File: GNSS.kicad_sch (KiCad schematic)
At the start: 0 parts

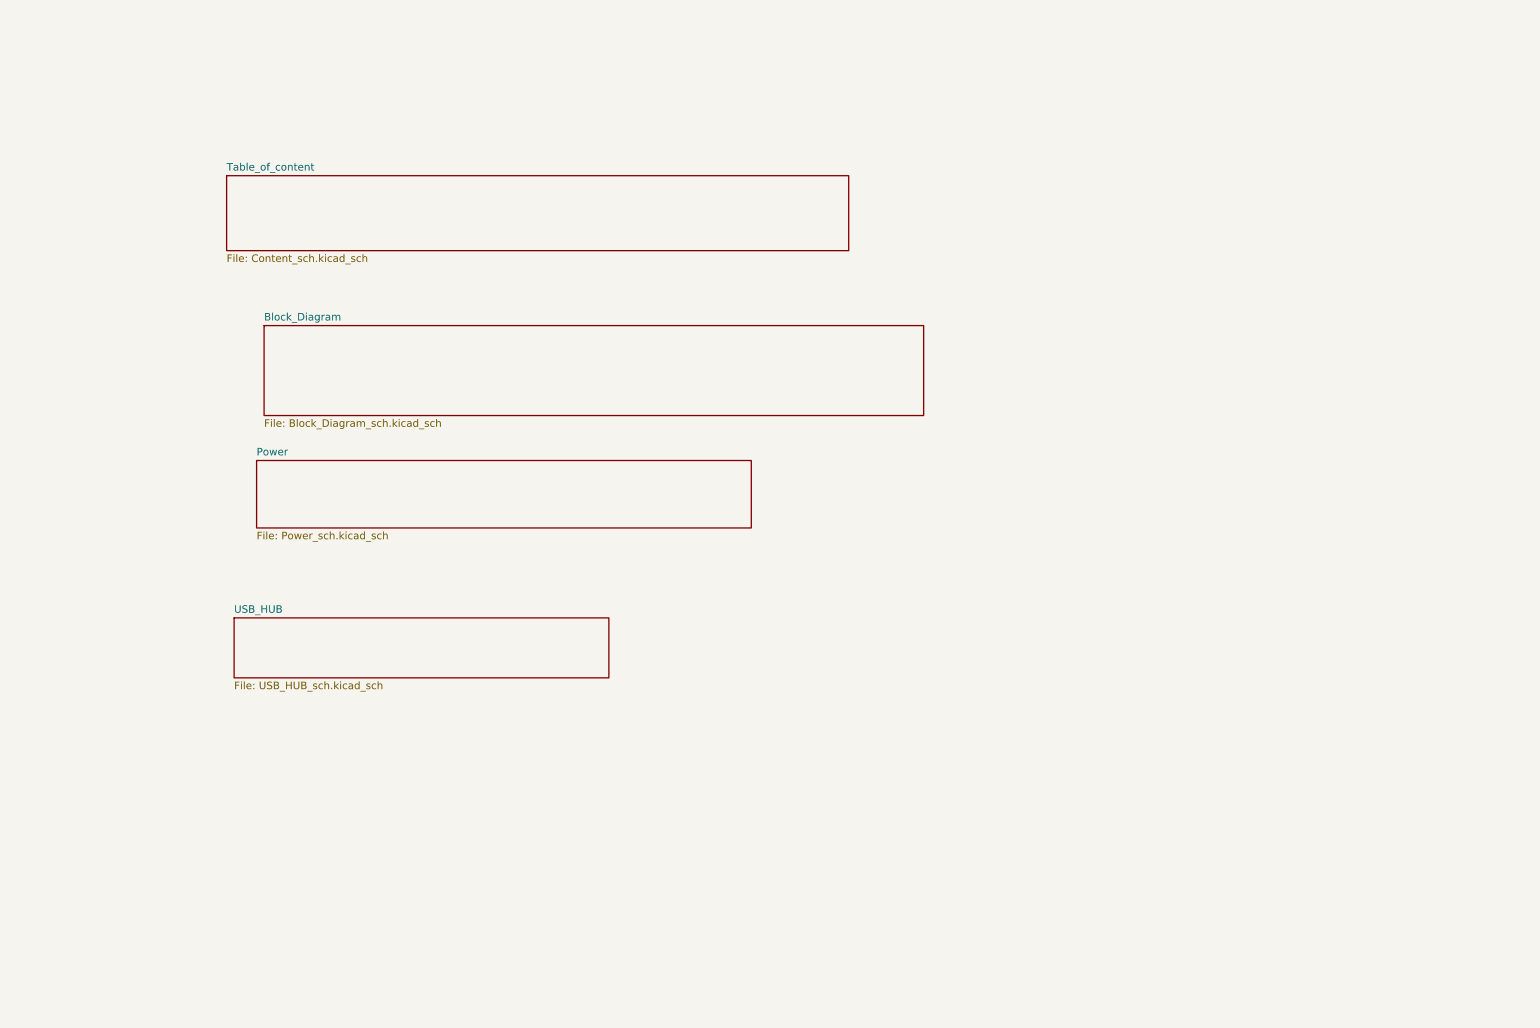
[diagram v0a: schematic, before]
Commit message: update the power sheet
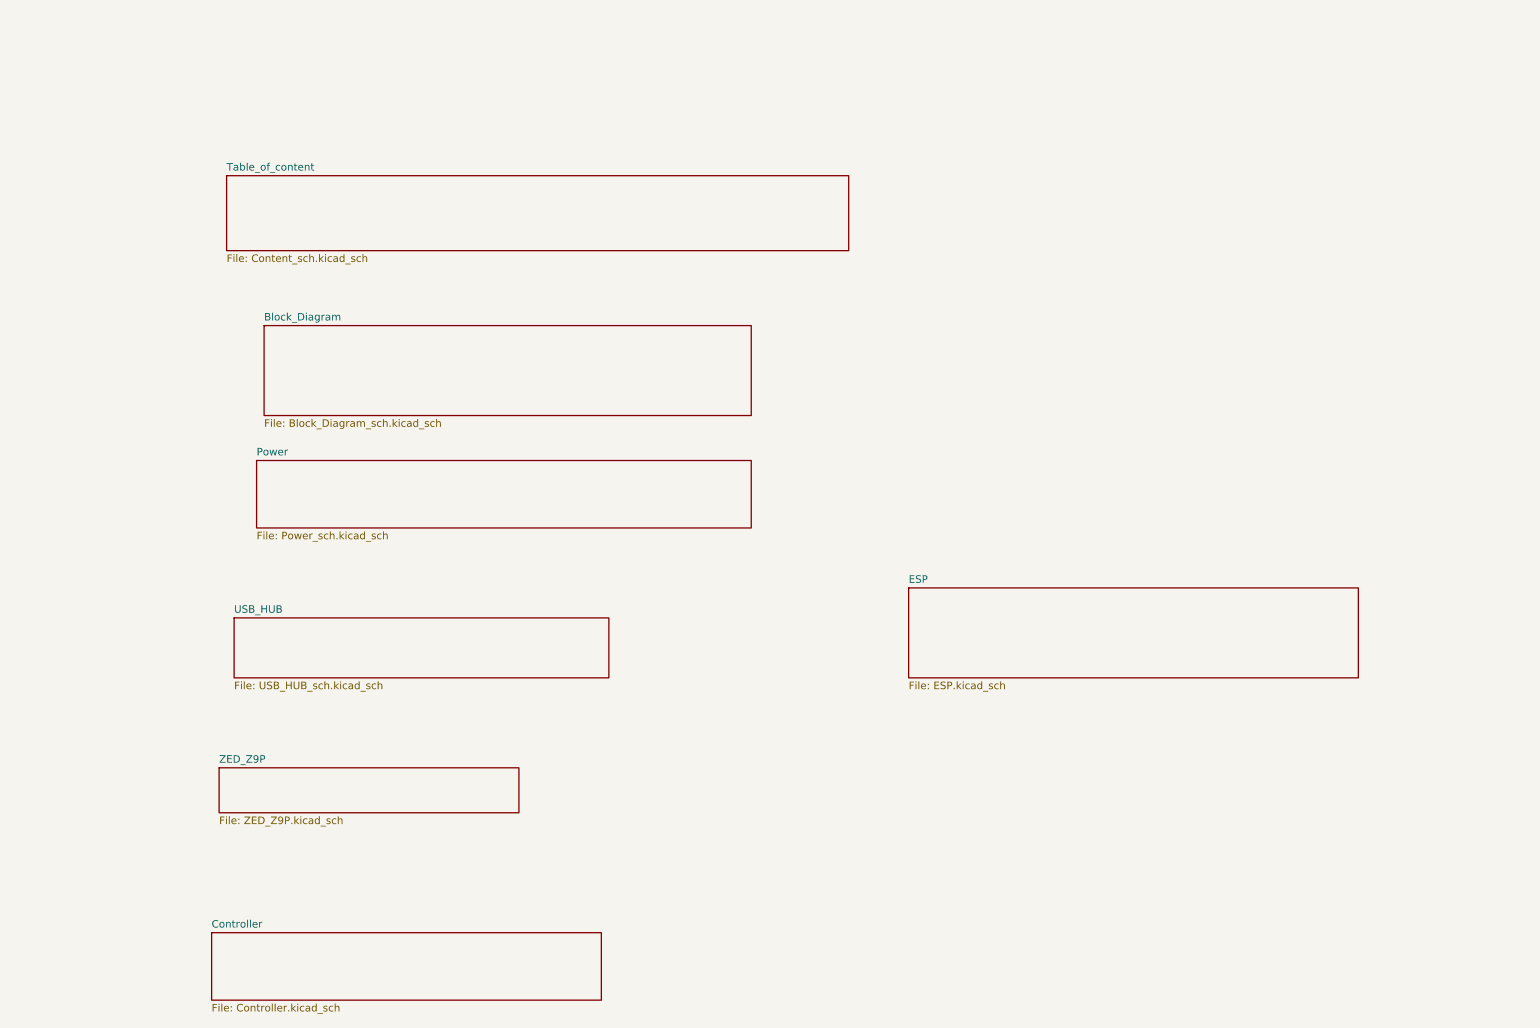
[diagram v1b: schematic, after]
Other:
- added sheet Controller (Controller.kicad_sch)
- added sheet ESP (ESP.kicad_sch)
- added sheet ZED_Z9P (ZED_Z9P.kicad_sch)
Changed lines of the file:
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@@
+	)
+	(sheet
+		(at 55.88 143.51)
+		(size 50.8 7.62)
+		(fields_autoplaced yes)
+		(stroke
+			(width 0.1524)
+			(type solid)
+		)
+		(fill
+			(color 0 0 0 0.0000)
+		)
+		(property "Sheetname" "ZED_Z9P"
+			(at 55.88 142.7984 0)
+			(effects
+				(font
+					(size 1.27 1.27)
+				)
+				(justify left bottom)
+			)
+		)
+		(property "Sheetfile" "ZED_Z9P.kicad_sch"
+			(at 55.88 151.7146 0)
+			(effects
+				(font
+					(size 1.27 1.27)
+				)
+				(justify left top)
+			)
+		)
+		(instances
+			(project "GNSS"
+				(path "/a70dad34-b24c-4b58-b91c-f14576b5da7d"
+					(page "6")
+				)
+			)
+		)
 	)
 	(sheet
@@
 	)
 	(sheet
+		(at 54.61 171.45)
+		(size 66.04 11.43)
+		(fields_autoplaced yes)
+		(stroke
+			(width 0.1524)
+			(type solid)
+		)
+		(fill
+			(color 0 0 0 0.0000)
+		)
+		(property "Sheetname" "Controller"
+			(at 54.61 170.7384 0)
+			(effects
+				(font
+					(size 1.27 1.27)
+				)
+				(justify left bottom)
+			)
+		)
+		(property "Sheetfile" "Controller.kicad_sch"
+			(at 54.61 183.4646 0)
+			(effects
+				(font
+					(size 1.27 1.27)
+				)
+				(justify left top)
+			)
+		)
+		(instances
+			(project "GNSS"
+				(path "/a70dad34-b24c-4b58-b91c-f14576b5da7d"
+					(page "7")
+				)
+			)
+		)
+	)
+	(sheet
 		(at 63.5 68.58)
-		(size 111.76 15.24)
+		(size 82.55 15.24)
 		(fields_autoplaced yes)
 		(stroke
@@
 				)
 			)
+		)
+	)
+	(sheet
+		(at 172.72 113.03)
+		(size 76.2 15.24)
+		(fields_autoplaced yes)
+		(stroke
+			(width 0.1524)
+			(type solid)
+		)
+		(fill
+			(color 0 0 0 0.0000)
+		)
+		(property "Sheetname" "ESP"
+			(at 172.72 112.3184 0)
+			(effects
+				(font
+					(size 1.27 1.27)
+				)
+				(justify left bottom)
+			)
+		)
+		(property "Sheetfile" "ESP.kicad_sch"
+			(at 172.72 128.8546 0)
+			(effects
+				(font
+					(size 1.27 1.27)
+				)
+				(justify left top)
+			)
+		)
+		(instances
+			(project "GNSS"
+				(path "/a70dad34-b24c-4b58-b91c-f14576b5da7d"
+					(page "8")
+				)
+			)

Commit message: arrange the Sheets
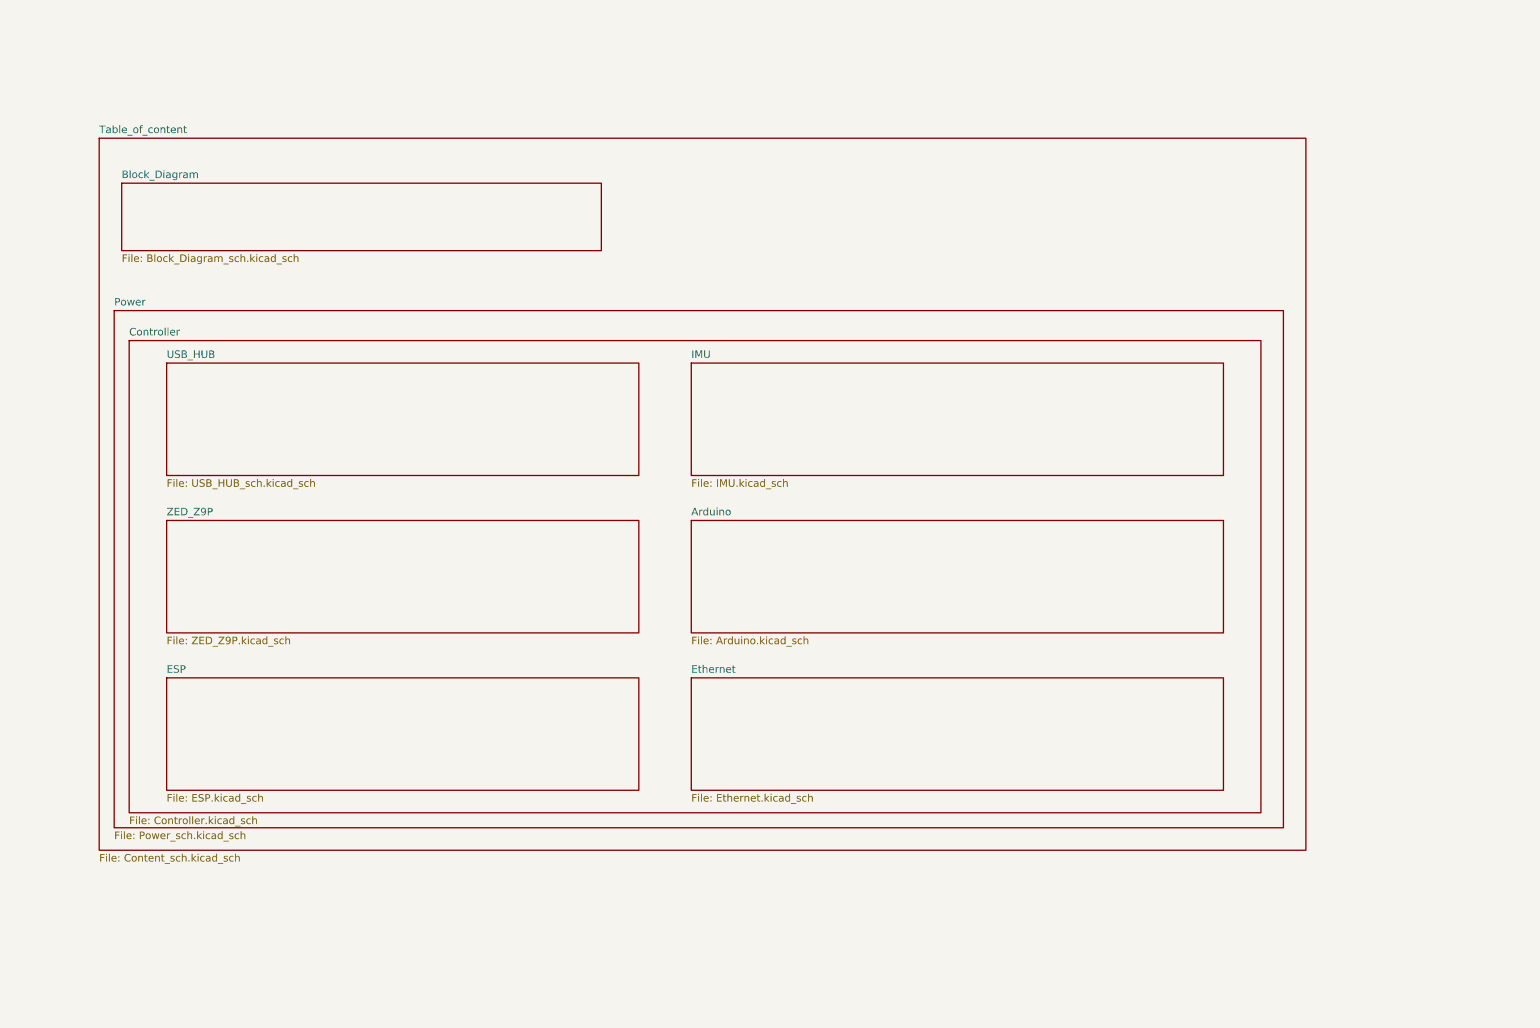
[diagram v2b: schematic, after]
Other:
- added sheet Arduino (Arduino.kicad_sch)
- added sheet Ethernet (Ethernet.kicad_sch)
- added sheet IMU (IMU.kicad_sch)
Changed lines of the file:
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@@
 	(paper "A4")
 	(sheet
-		(at 57.15 43.18)
-		(size 105.41 12.7)
+		(at 35.56 36.83)
+		(size 204.47 120.65)
 		(fields_autoplaced yes)
 		(stroke
@@
 		)
 		(property "Sheetname" "Table_of_content"
-			(at 57.15 42.4684 0)
+			(at 35.56 36.1184 0)
 			(effects
 				(font
@@
 		)
 		(property "Sheetfile" "Content_sch.kicad_sch"
-			(at 57.15 56.4646 0)
+			(at 35.56 158.0646 0)
 			(effects
 				(font
@@
 	)
 	(sheet
-		(at 55.88 143.51)
-		(size 50.8 7.62)
+		(at 135.89 74.93)
+		(size 90.17 19.05)
+		(fields_autoplaced yes)
+		(stroke
+			(width 0.1524)
+			(type solid)
+		)
+		(fill
+			(color 0 0 0 0.0000)
+		)
+		(property "Sheetname" "IMU"
+			(at 135.89 74.2184 0)
+			(effects
+				(font
+					(size 1.27 1.27)
+				)
+				(justify left bottom)
+			)
+		)
+		(property "Sheetfile" "IMU.kicad_sch"
+			(at 135.89 94.5646 0)
+			(effects
+				(font
+					(size 1.27 1.27)
+				)
+				(justify left top)
+			)
+		)
+		(instances
+			(project "GNSS"
+				(path "/a70dad34-b24c-4b58-b91c-f14576b5da7d"
+					(page "11")
+				)
+			)
+		)
+	)
+	(sheet
+		(at 46.99 101.6)
+		(size 80.01 19.05)
 		(fields_autoplaced yes)
 		(stroke
@@
 		)
 		(property "Sheetname" "ZED_Z9P"
-			(at 55.88 142.7984 0)
+			(at 46.99 100.8884 0)
 			(effects
 				(font
@@
 		)
 		(property "Sheetfile" "ZED_Z9P.kicad_sch"
-			(at 55.88 151.7146 0)
+			(at 46.99 121.2346 0)
 			(effects
 				(font
@@
 	)
 	(sheet
-		(at 58.42 118.11)
-		(size 63.5 10.16)
+		(at 46.99 74.93)
+		(size 80.01 19.05)
 		(fields_autoplaced yes)
 		(stroke
@@
 		)
 		(property "Sheetname" "USB_HUB"
-			(at 58.42 117.3984 0)
+			(at 46.99 74.2184 0)
 			(effects
 				(font
@@
 		)
 		(property "Sheetfile" "USB_HUB_sch.kicad_sch"
-			(at 58.42 128.8546 0)
+			(at 46.99 94.5646 0)
 			(effects
 				(font
@@
 	)
 	(sheet
-		(at 54.61 171.45)
-		(size 66.04 11.43)
+		(at 40.64 71.12)
+		(size 191.77 80.01)
 		(fields_autoplaced yes)
 		(stroke
@@
 		)
 		(property "Sheetname" "Controller"
-			(at 54.61 170.7384 0)
+			(at 40.64 70.4084 0)
 			(effects
 				(font
@@
 		)
 		(property "Sheetfile" "Controller.kicad_sch"
-			(at 54.61 183.4646 0)
+			(at 40.64 151.7146 0)
 			(effects
 				(font
@@
 	)
 	(sheet
-		(at 63.5 68.58)
-		(size 82.55 15.24)
+		(at 39.37 44.45)
+		(size 81.28 11.43)
 		(fields_autoplaced yes)
 		(stroke
@@
 		)
 		(property "Sheetname" "Block_Diagram"
-			(at 63.5 67.8684 0)
+			(at 39.37 43.7384 0)
 			(effects
 				(font
@@
 		)
 		(property "Sheetfile" "Block_Diagram_sch.kicad_sch"
-			(at 63.5 84.4046 0)
+			(at 39.37 56.4646 0)
 			(effects
 				(font
@@
 	)
 	(sheet
-		(at 62.23 91.44)
-		(size 83.82 11.43)
+		(at 38.1 66.04)
+		(size 198.12 87.63)
 		(fields_autoplaced yes)
 		(stroke
@@
 		)
 		(property "Sheetname" "Power"
-			(at 62.23 90.7284 0)
+			(at 38.1 65.3284 0)
 			(effects
 				(font
@@
 		)
 		(property "Sheetfile" "Power_sch.kicad_sch"
-			(at 62.23 103.4546 0)
+			(at 38.1 154.2546 0)
 			(effects
 				(font
@@
 	)
 	(sheet
-		(at 172.72 113.03)
-		(size 76.2 15.24)
+		(at 135.89 128.27)
+		(size 90.17 19.05)
+		(fields_autoplaced yes)
+		(stroke
+			(width 0.1524)
+			(type solid)
+		)
+		(fill
+			(color 0 0 0 0.0000)
+		)
+		(property "Sheetname" "Ethernet"
+			(at 135.89 127.5584 0)
+			(effects
+				(font
+					(size 1.27 1.27)
+				)
+				(justify left bottom)
+			)
+		)
+		(property "Sheetfile" "Ethernet.kicad_sch"
+			(at 135.89 147.9046 0)
+			(effects
+				(font
+					(size 1.27 1.27)
+				)
+				(justify left top)
+			)
+		)
+		(instances
+			(project "GNSS"
+				(path "/a70dad34-b24c-4b58-b91c-f14576b5da7d"
+					(page "10")
+				)
+			)
+		)
+	)
+	(sheet
+		(at 135.89 101.6)
+		(size 90.17 19.05)
+		(fields_autoplaced yes)
+		(stroke
+			(width 0.1524)
+			(type solid)
+		)
+		(fill
+			(color 0 0 0 0.0000)
+		)
+		(property "Sheetname" "Arduino"
+			(at 135.89 100.8884 0)
+			(effects
+				(font
+					(size 1.27 1.27)
+				)
+				(justify left bottom)
+			)
+		)
+		(property "Sheetfile" "Arduino.kicad_sch"
+			(at 135.89 121.2346 0)
+			(effects
+				(font
+					(size 1.27 1.27)
+				)
+				(justify left top)
+			)
+		)
+		(instances
+			(project "GNSS"
+				(path "/a70dad34-b24c-4b58-b91c-f14576b5da7d"
+					(page "9")
+				)
+			)
+		)
+	)
+	(sheet
+		(at 46.99 128.27)
+		(size 80.01 19.05)
 		(fields_autoplaced yes)
 		(stroke
@@
 		)
 		(property "Sheetname" "ESP"
-			(at 172.72 112.3184 0)
+			(at 46.99 127.5584 0)
 			(effects
 				(font
@@
 		)
 		(property "Sheetfile" "ESP.kicad_sch"
-			(at 172.72 128.8546 0)
-			(effects
-				(font
+			(at 46.99 147.9046 0)
+			(effects
+				(font

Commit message: new
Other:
- added sheet Power_Architecture (Power_Architecture.kicad_sch)
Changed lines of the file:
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@@
 	(paper "A4")
 	(sheet
-		(at 35.56 36.83)
-		(size 204.47 120.65)
+		(at 36.83 21.59)
+		(size 204.47 137.16)
 		(fields_autoplaced yes)
 		(stroke
@@
 		)
 		(property "Sheetname" "Table_of_content"
-			(at 35.56 36.1184 0)
+			(at 36.83 20.8784 0)
 			(effects
 				(font
@@
 		)
 		(property "Sheetfile" "Content_sch.kicad_sch"
-			(at 35.56 158.0646 0)
+			(at 36.83 159.3346 0)
 			(effects
 				(font
@@
 	)
 	(sheet
-		(at 135.89 74.93)
+		(at 137.16 74.93)
 		(size 90.17 19.05)
 		(fields_autoplaced yes)
@@
 		)
 		(property "Sheetname" "IMU"
-			(at 135.89 74.2184 0)
+			(at 137.16 74.2184 0)
 			(effects
 				(font
@@
 		)
 		(property "Sheetfile" "IMU.kicad_sch"
-			(at 135.89 94.5646 0)
+			(at 137.16 94.5646 0)
 			(effects
 				(font
@@
 	)
 	(sheet
-		(at 46.99 101.6)
+		(at 48.26 101.6)
 		(size 80.01 19.05)
 		(fields_autoplaced yes)
@@
 		)
 		(property "Sheetname" "ZED_Z9P"
-			(at 46.99 100.8884 0)
+			(at 48.26 100.8884 0)
 			(effects
 				(font
@@
 		)
 		(property "Sheetfile" "ZED_Z9P.kicad_sch"
-			(at 46.99 121.2346 0)
+			(at 48.26 121.2346 0)
 			(effects
 				(font
@@
 	)
 	(sheet
-		(at 46.99 74.93)
+		(at 48.26 74.93)
 		(size 80.01 19.05)
 		(fields_autoplaced yes)
@@
 		)
 		(property "Sheetname" "USB_HUB"
-			(at 46.99 74.2184 0)
+			(at 48.26 74.2184 0)
 			(effects
 				(font
@@
 		)
 		(property "Sheetfile" "USB_HUB_sch.kicad_sch"
-			(at 46.99 94.5646 0)
+			(at 48.26 94.5646 0)
 			(effects
 				(font
@@
 	)
 	(sheet
-		(at 40.64 71.12)
+		(at 43.18 53.34)
+		(size 71.12 11.43)
+		(fields_autoplaced yes)
+		(stroke
+			(width 0.1524)
+			(type solid)
+		)
+		(fill
+			(color 0 0 0 0.0000)
+		)
+		(property "Sheetname" "Power_Architecture"
+			(at 43.18 52.6284 0)
+			(effects
+				(font
+					(size 1.27 1.27)
+				)
+				(justify left bottom)
+			)
+		)
+		(property "Sheetfile" "Power_Architecture.kicad_sch"
+			(at 43.18 65.3546 0)
+			(effects
+				(font
+					(size 1.27 1.27)
+				)
+				(justify left top)
+			)
+		)
+		(instances
+			(project "GNSS"
+				(path "/a70dad34-b24c-4b58-b91c-f14576b5da7d"
+					(page "12")
+				)
+			)
+		)
+	)
+	(sheet
+		(at 41.91 71.12)
 		(size 191.77 80.01)
 		(fields_autoplaced yes)
@@
 		)
 		(property "Sheetname" "Controller"
-			(at 40.64 70.4084 0)
+			(at 41.91 70.4084 0)
 			(effects
 				(font
@@
 		)
 		(property "Sheetfile" "Controller.kicad_sch"
-			(at 40.64 151.7146 0)
+			(at 41.91 151.7146 0)
 			(effects
 				(font
@@
 	)
 	(sheet
-		(at 39.37 44.45)
+		(at 40.64 26.67)
 		(size 81.28 11.43)
 		(fields_autoplaced yes)
@@
 		)
 		(property "Sheetname" "Block_Diagram"
-			(at 39.37 43.7384 0)
+			(at 40.64 25.9584 0)
 			(effects
 				(font
@@
 		)
 		(property "Sheetfile" "Block_Diagram_sch.kicad_sch"
-			(at 39.37 56.4646 0)
+			(at 40.64 38.6846 0)
 			(effects
 				(font
@@
 	)
 	(sheet
-		(at 38.1 66.04)
-		(size 198.12 87.63)
+		(at 39.37 46.99)
+		(size 198.12 106.68)
 		(fields_autoplaced yes)
 		(stroke
@@
 		)
 		(property "Sheetname" "Power"
-			(at 38.1 65.3284 0)
+			(at 39.37 46.2784 0)
 			(effects
 				(font
@@
 		)
 		(property "Sheetfile" "Power_sch.kicad_sch"
-			(at 38.1 154.2546 0)
+			(at 39.37 154.2546 0)
 			(effects
 				(font
@@
 	)
 	(sheet
-		(at 135.89 128.27)
+		(at 137.16 128.27)
 		(size 90.17 19.05)
 		(fields_autoplaced yes)
@@
 		)
 		(property "Sheetname" "Ethernet"
-			(at 135.89 127.5584 0)
+			(at 137.16 127.5584 0)
 			(effects
 				(font
@@
 		)
 		(property "Sheetfile" "Ethernet.kicad_sch"
-			(at 135.89 147.9046 0)
+			(at 137.16 147.9046 0)
 			(effects
 				(font
@@
 	)
 	(sheet
-		(at 135.89 101.6)
+		(at 137.16 101.6)
 		(size 90.17 19.05)
 		(fields_autoplaced yes)
@@
 		)
 		(property "Sheetname" "Arduino"
-			(at 135.89 100.8884 0)
+			(at 137.16 100.8884 0)
 			(effects
 				(font
@@
 		)
 		(property "Sheetfile" "Arduino.kicad_sch"
-			(at 135.89 121.2346 0)
+			(at 137.16 121.2346 0)
 			(effects
 				(font
@@
 	)
 	(sheet
-		(at 46.99 128.27)
+		(at 48.26 128.27)
 		(size 80.01 19.05)
 		(fields_autoplaced yes)
@@
 		)
 		(property "Sheetname" "ESP"
-			(at 46.99 127.5584 0)
+			(at 48.26 127.5584 0)
 			(effects
 				(font
@@
 		)
 		(property "Sheetfile" "ESP.kicad_sch"
-			(at 46.99 147.9046 0)
-			(effects
-				(font
+			(at 48.26 147.9046 0)
+			(effects
+				(font
